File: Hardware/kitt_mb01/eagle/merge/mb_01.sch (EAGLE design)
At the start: 112 parts, among them CON1 ARDUINO_UNO, IC1.01 RT8293A, IC2.00 BQ24266RGET, IC3.01 LSM9DS1, P2 S2B-PH-K-S(LF)(SN), U6.01 TPS61032RSARPSDO-G16, U7.01 SI1922EDH, X7.02 HEAD-LIGHT, X7.03 TAIL-LIGHT, X7.05 MOTOR

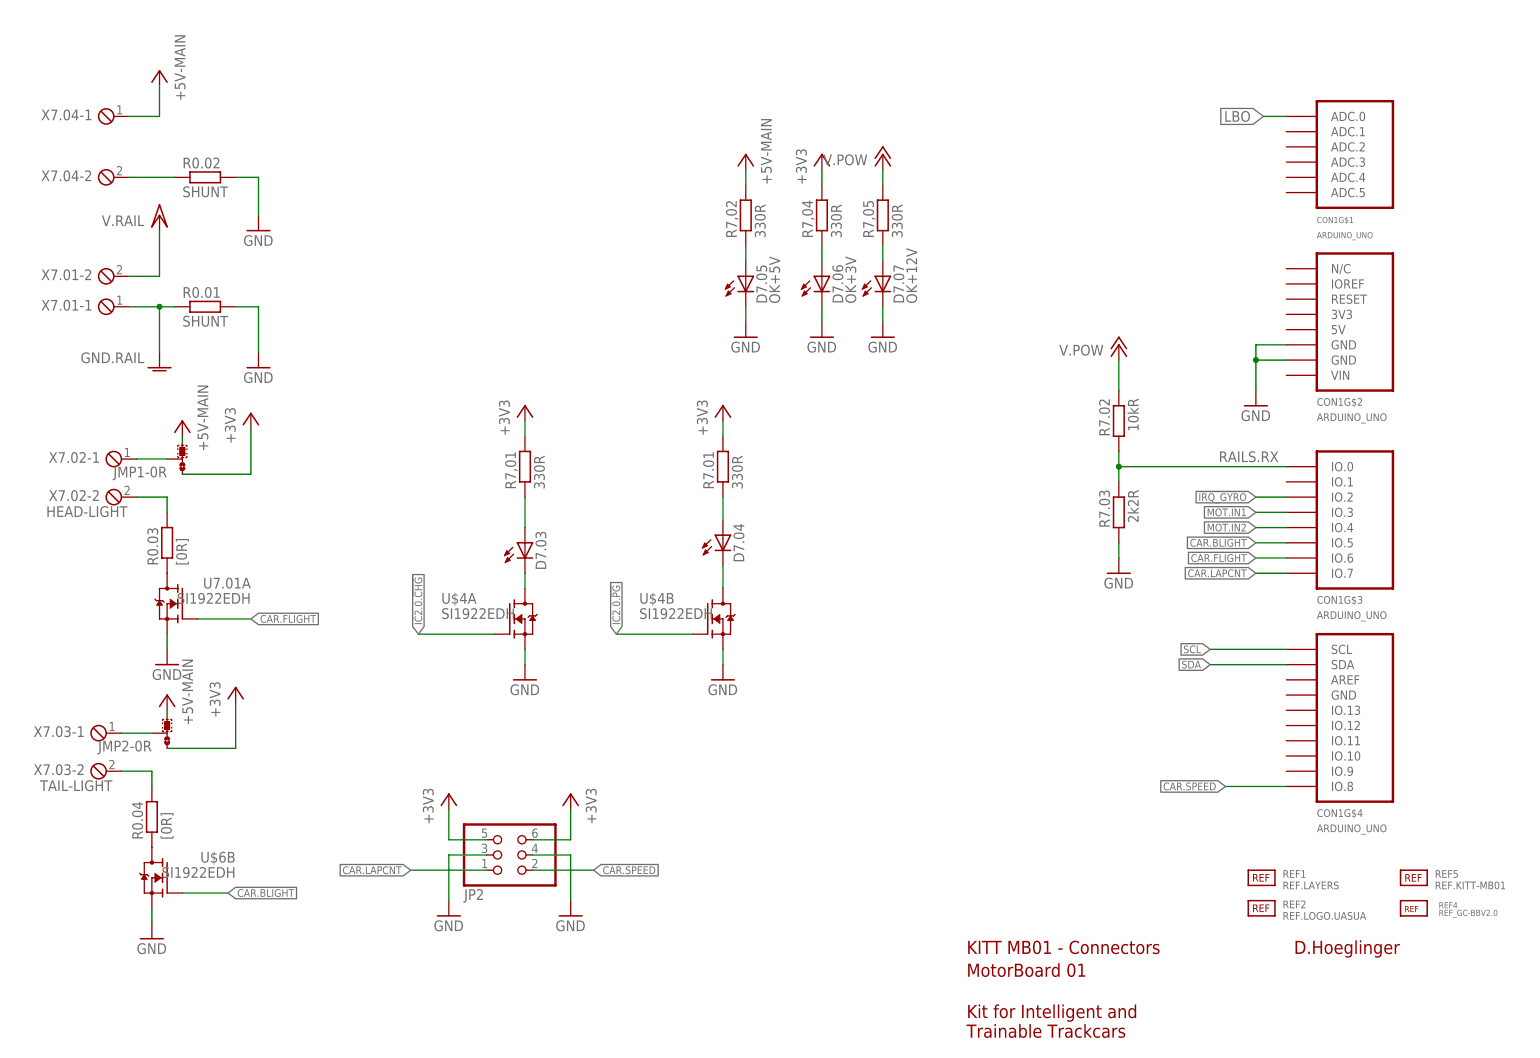
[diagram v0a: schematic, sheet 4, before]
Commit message: snapshot of board merge : power edition
-> added patch-through of power rails to arduino connector
-> did some minor reroutes
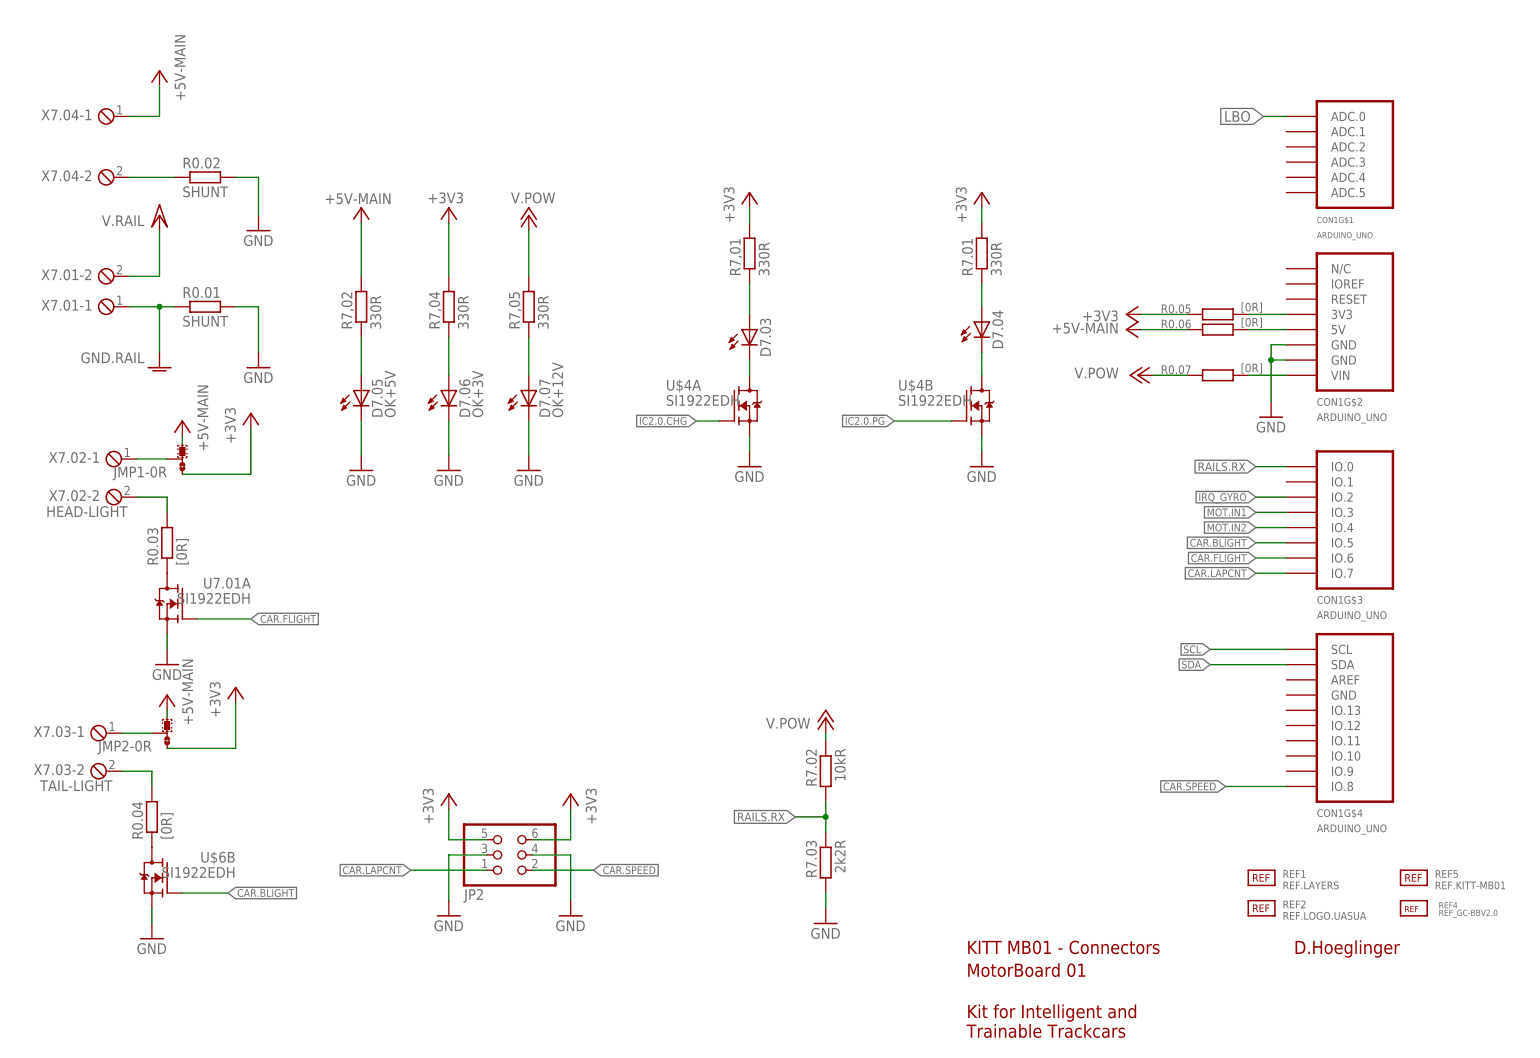
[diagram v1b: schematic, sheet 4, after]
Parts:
- removed R2.06: 10kR/NTC, ptc-ntc:V642
- added PTC+, PTC-: (no value), wirepad:SMD2
- added R0.05, R0.06, R0.07: [0R], rcl:R-EU_R1206
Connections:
- new net N$3: CON1G$2.3V3, R0.05.2
- new net N$4: CON1G$2.5V, R0.06.2
- new net N$5: CON1G$2.VIN, R0.07.2
- net +12V: now also R0.07.1
- net +3V3: now also R0.05.1
- net +5V: now also R0.06.1
- net GND: now also PTC-.P; no longer R2.06.1
- net N$15: now also PTC+.P; no longer R2.06.2
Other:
- moved on the sheet: D7.03, D7.04, D7.05, D7.06, D7.07, R2.08, R7,01, R7,02, R7,04, R7,05, R7.01, R7.02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

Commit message: board merge snapshot : pretty satisfactory edition -> added/utilized both LED FET gates by using SMT break headers -> this included the GATE_LED for controlling the track -> obligatory reroutes were made
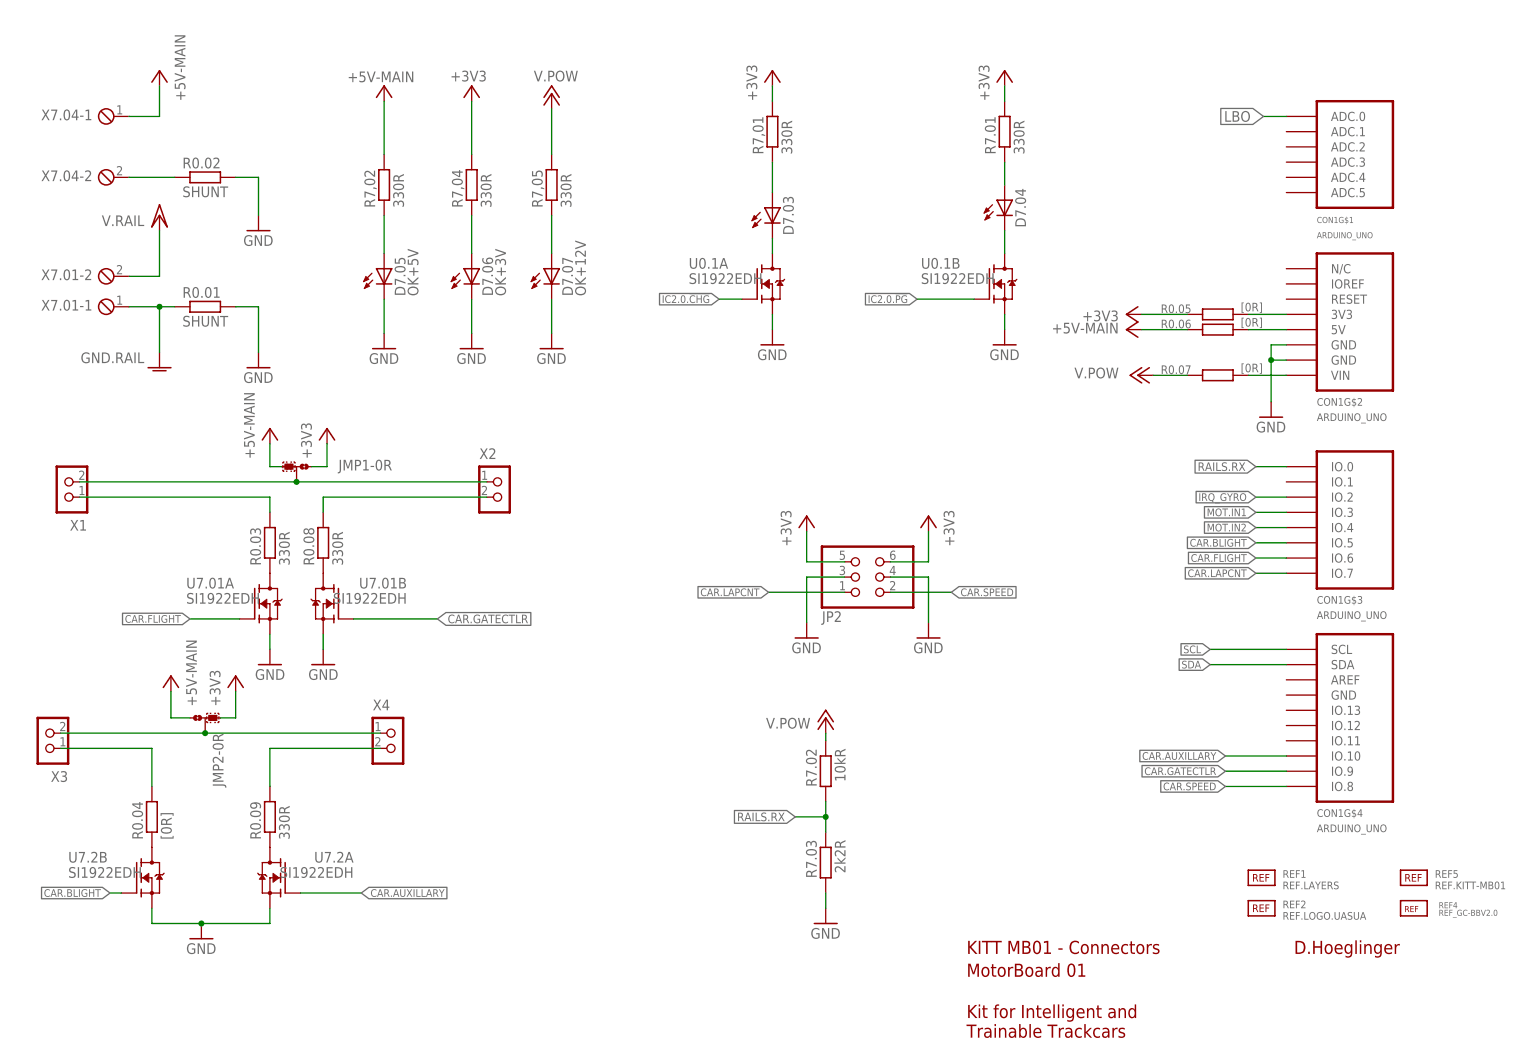
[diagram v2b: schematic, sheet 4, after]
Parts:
- removed U$4, U$6: SI1922EDH, kitt.ic:SI1922EDH
- removed X7.02: HEAD-LIGHT, con-phoenix-254:MPT2
- removed X7.03: TAIL-LIGHT, con-phoenix-254:MPT2
- added R0.08, R0.09: 330R, rcl:R-EU_R1206
- added U0.1, U7.2: SI1922EDH, kitt.ic:SI1922EDH
- added X1, X2, X3, X4: CON_HEADER_1X02, kitt.con:CON_HEADER_1X02
- R0.03: value [0R] -> 330R
- renumbered PTC+ to NTC+, PTC- to NTC-
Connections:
- new net CAR.AUXILLARY: CON1G$4.IO.10, U7.2A.G
- new net CAR.GATECTLR: CON1G$4.IO.9, U7.01B.G
- new net N$50: R0.08.2, X2.2
- new net N$51: R0.09.1, U7.2A.D
- new net N$52: R0.09.2, X4.2
- new net N$7: R0.08.1, U7.01B.D
- net CAR.BLIGHT: now also U7.2B.G; no longer U$6B.G
- net GND: now also U0.1A.S, U0.1B.S, U7.01B.S, U7.2A.S, U7.2B.S; no longer U$4A.S, U$4B.S, U$6B.S
- net IC2.0.!CHG: now also U0.1A.G; no longer U$4A.G
- net IC2.0.!PG: now also U0.1B.G; no longer U$4B.G
- net N$28: now also U0.1A.D; no longer U$4A.D
- net N$31: now also U0.1B.D; no longer U$4B.D
- net N$42: now also X1.1; no longer X7.02-2.1
- net N$45: now also X1.2, X2.1; no longer X7.02-1.1
- net N$46: now also X3.1; no longer X7.03-2.1
- net N$47: now also U7.2B.D; no longer U$6B.D
- net N$48: now also X3.2, X4.1; no longer X7.03-1.1
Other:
- moved on the sheet: D7.03, D7.04, D7.05, D7.06, D7.07, JMP1-0R, JMP2-0R, JP2, R0.03, R7,01, R7,02, R7,04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

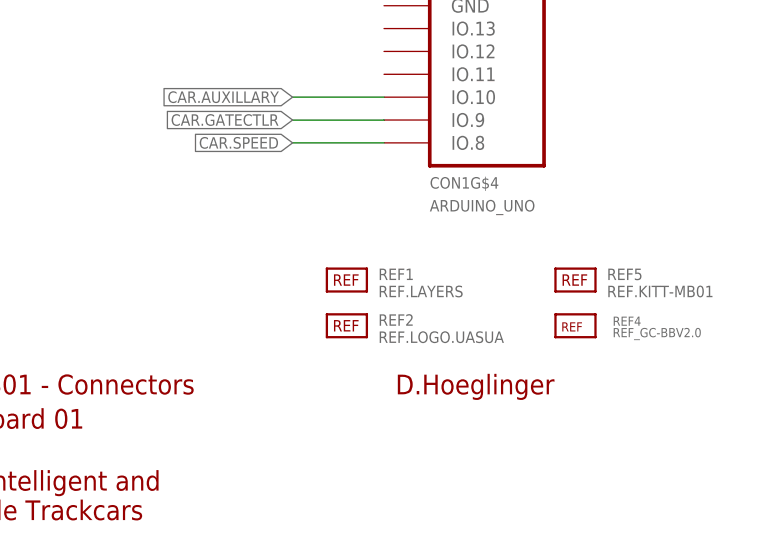
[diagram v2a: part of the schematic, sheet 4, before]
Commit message: board merge snapshot : semivalid edition -> ran through first DRC for Würth standard manufacture -> corrected 262 errors
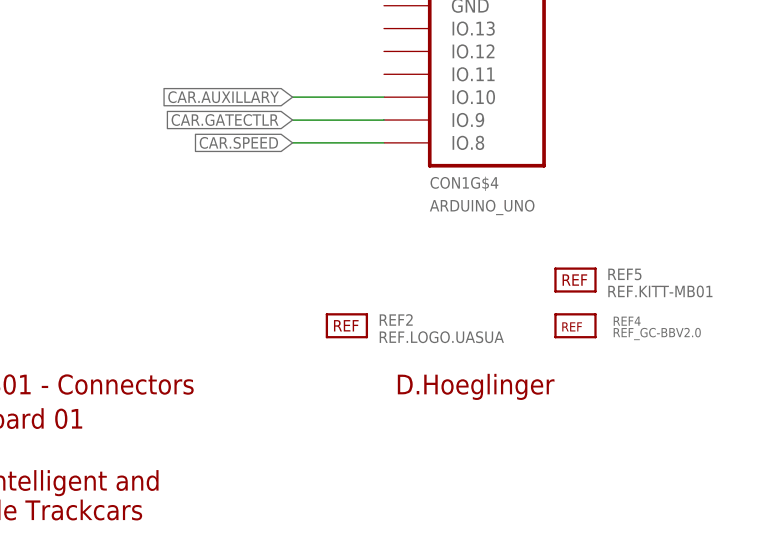
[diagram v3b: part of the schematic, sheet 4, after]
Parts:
- removed REF1: REF.LAYERS, kitt.refs:REF.LAYERS
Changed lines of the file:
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@@
 <part name="D7.07" library="led" deviceset="LED" device="CHIPLED_1206" value="OK+12V"/>
 <part name="GND37" library="supply1" deviceset="GND" device=""/>
-<part name="REF1" library="kitt.refs" deviceset="REF.LAYERS" device=""/>
 <part name="REF2" library="kitt.refs" deviceset="REF.LOGO.UASUA" device=""/>
 <part name="NTC+" library="wirepad" deviceset="SMD2" device=""/>
@@
 <instance part="D7.07" gate="G$1" x="93.345" y="134.62"/>
 <instance part="GND37" gate="1" x="93.345" y="121.285"/>
-<instance part="REF1" gate="G$1" x="209.55" y="31.75"/>
 <instance part="REF2" gate="G$1" x="209.55" y="26.67"/>
 <instance part="R0.05" gate="G$1" x="204.47" y="127" smashed="yes">

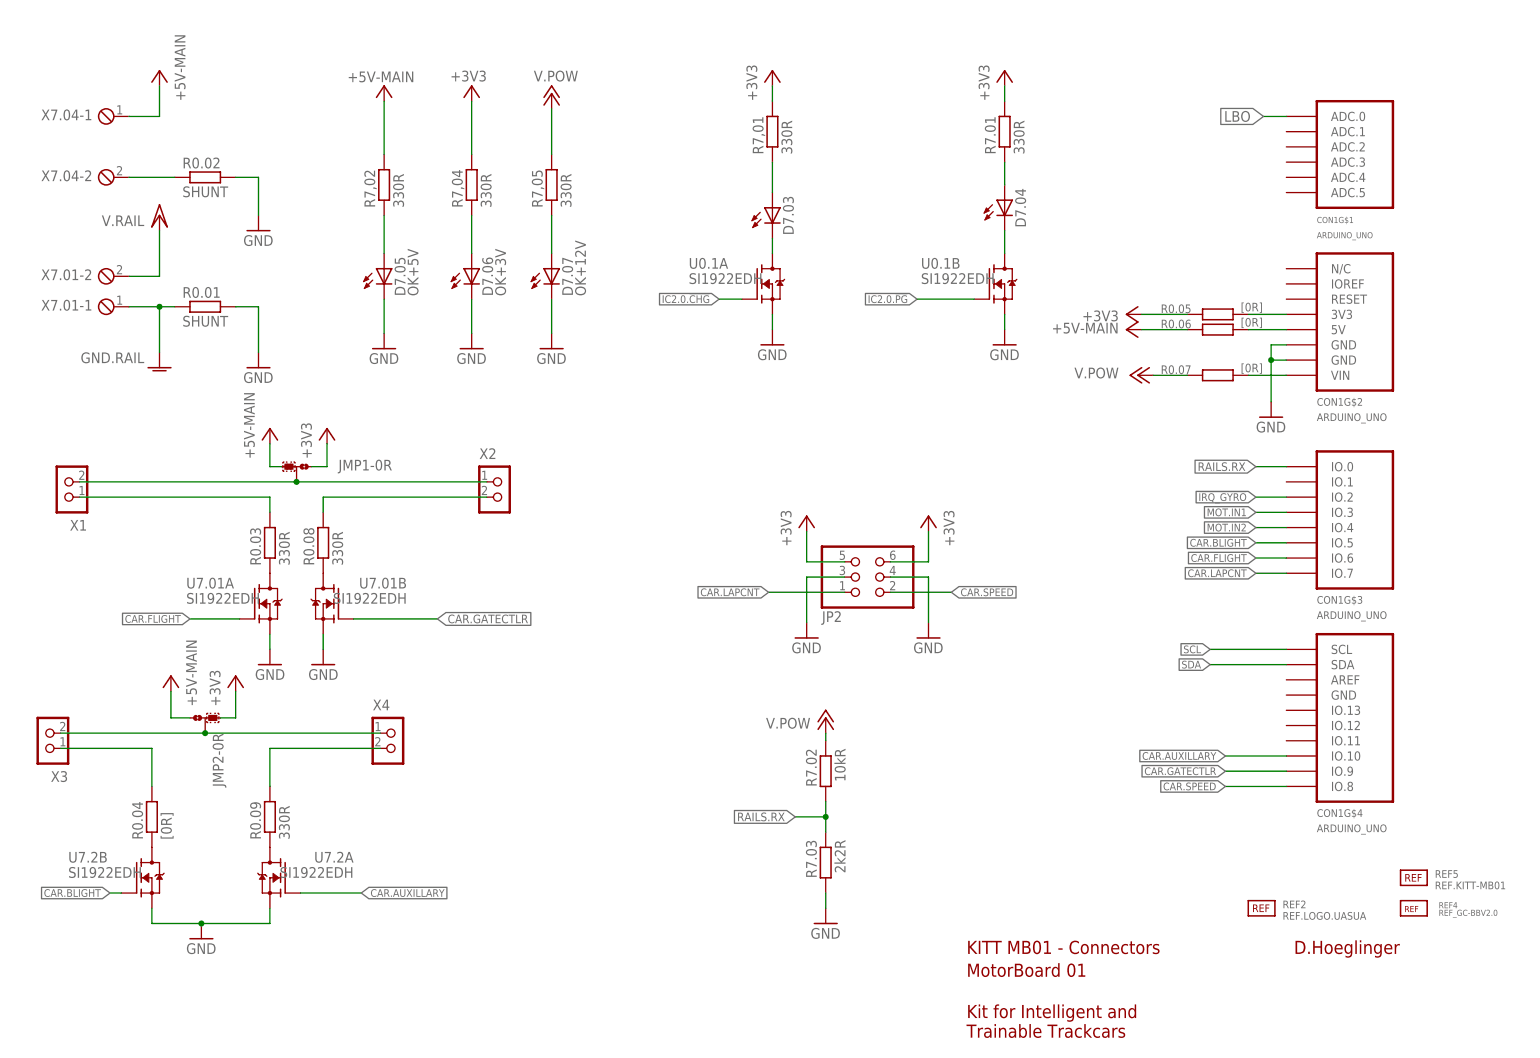
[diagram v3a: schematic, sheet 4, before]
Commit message: exported bill of materials, soon to be annotated with part# from vendors
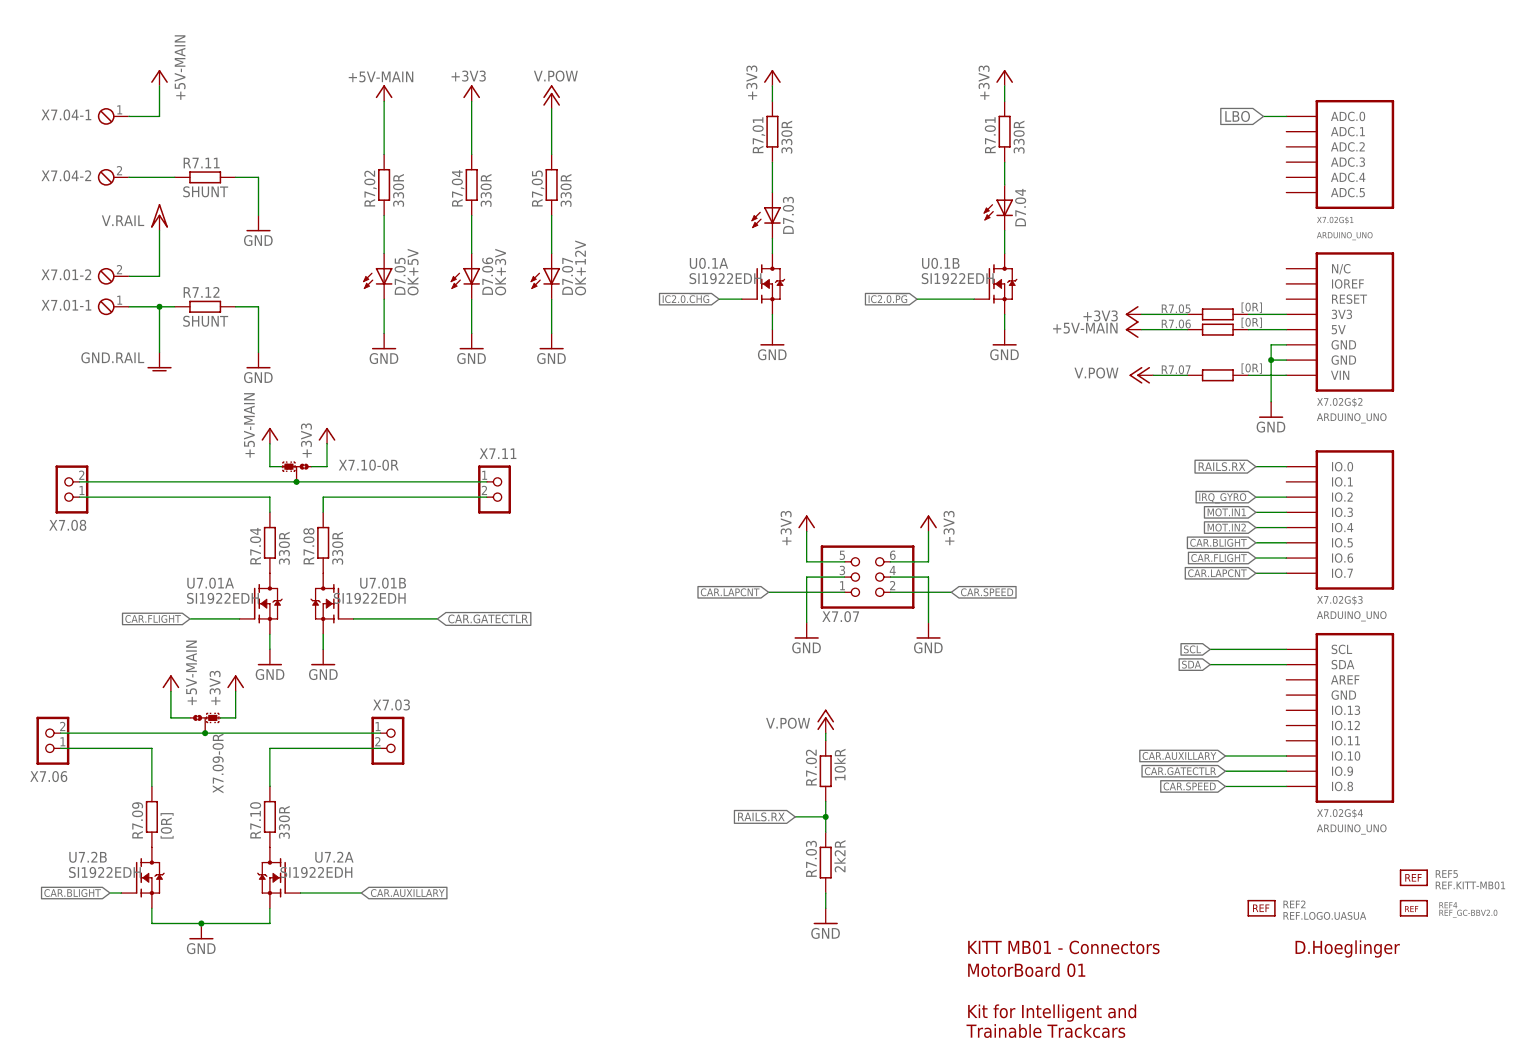
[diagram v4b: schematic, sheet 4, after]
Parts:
- renumbered CON1 to X7.02, D1 to D1.01, F1 to F1.01, IC1 to IC4.01, JMP1 to X7.10, JMP2 to X7.09, JP2 to X7.07, P2 to X2.01, Q1 to Q2.01, R0.01 to R7.12, R0.02 to R7.11, R0.03 to R7.04, R0.04 to R7.09, R0.05 to R7.05, R0.06 to R7.06, R0.07 to R7.07, R0.08 to R7.08, R0.09 to R7.10, SJ2 to J4.01, X1 to X7.08, X2 to X7.11, X3 to X7.06, X4 to X7.03
